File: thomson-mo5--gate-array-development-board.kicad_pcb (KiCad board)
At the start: 2 copper layers, 99.7 x 99.7 mm, 19 parts, among them J1 JTAG, J2 VPP connector, J3 5V->12V, J4 Adjustable MT3608 module, U1 4040, U2 4040, U3 GATE_ARRAY_MO5_V1_SOCKET, U4 GATE_ARRAY_MO5_V2_SOCKET, X1 XO 16MHz - DIP 8 or 14

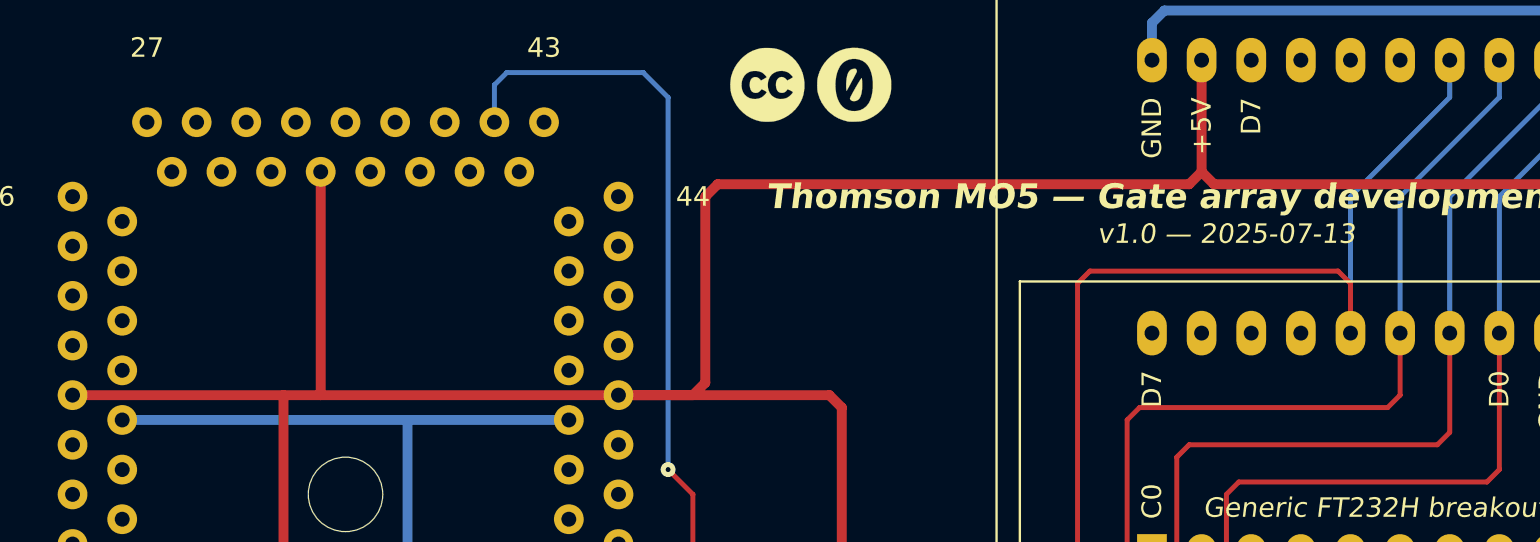
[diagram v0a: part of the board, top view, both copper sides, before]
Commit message: Fixed missing tie to ground for U3 pin 35
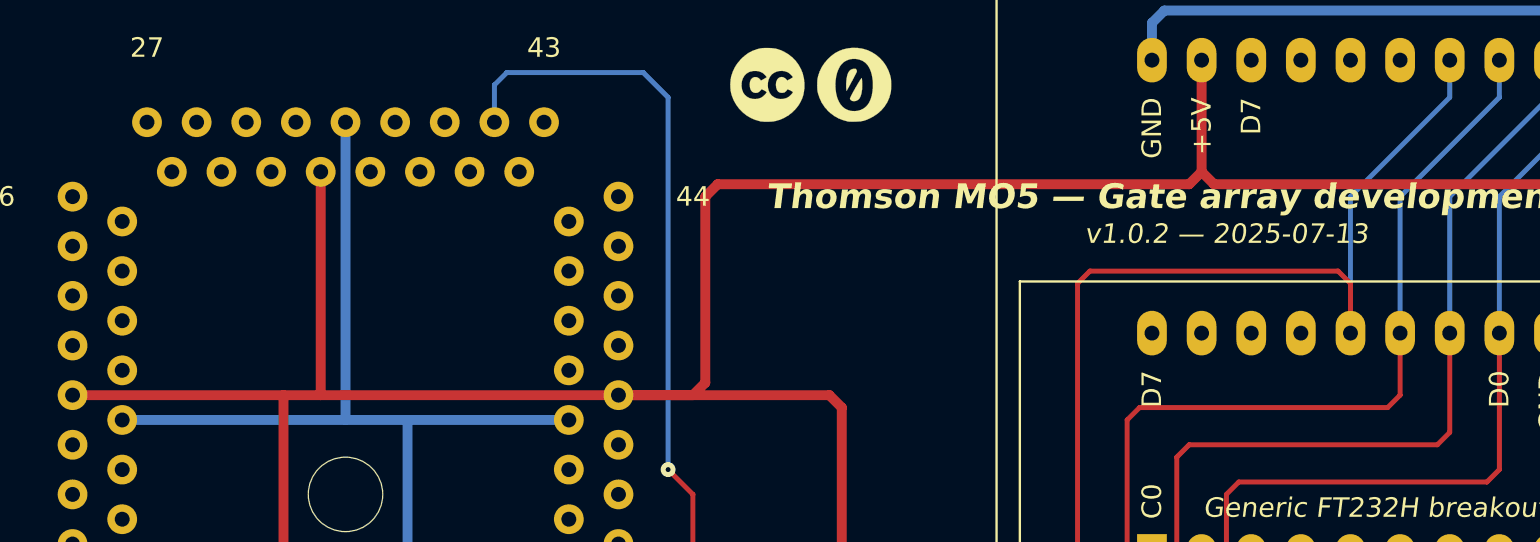
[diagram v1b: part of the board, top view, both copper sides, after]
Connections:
- U3 pad 35: unconnected-(U3-GND-Pad35) -> GND
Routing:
- net GND: track 333.4 -> 348.6 mm

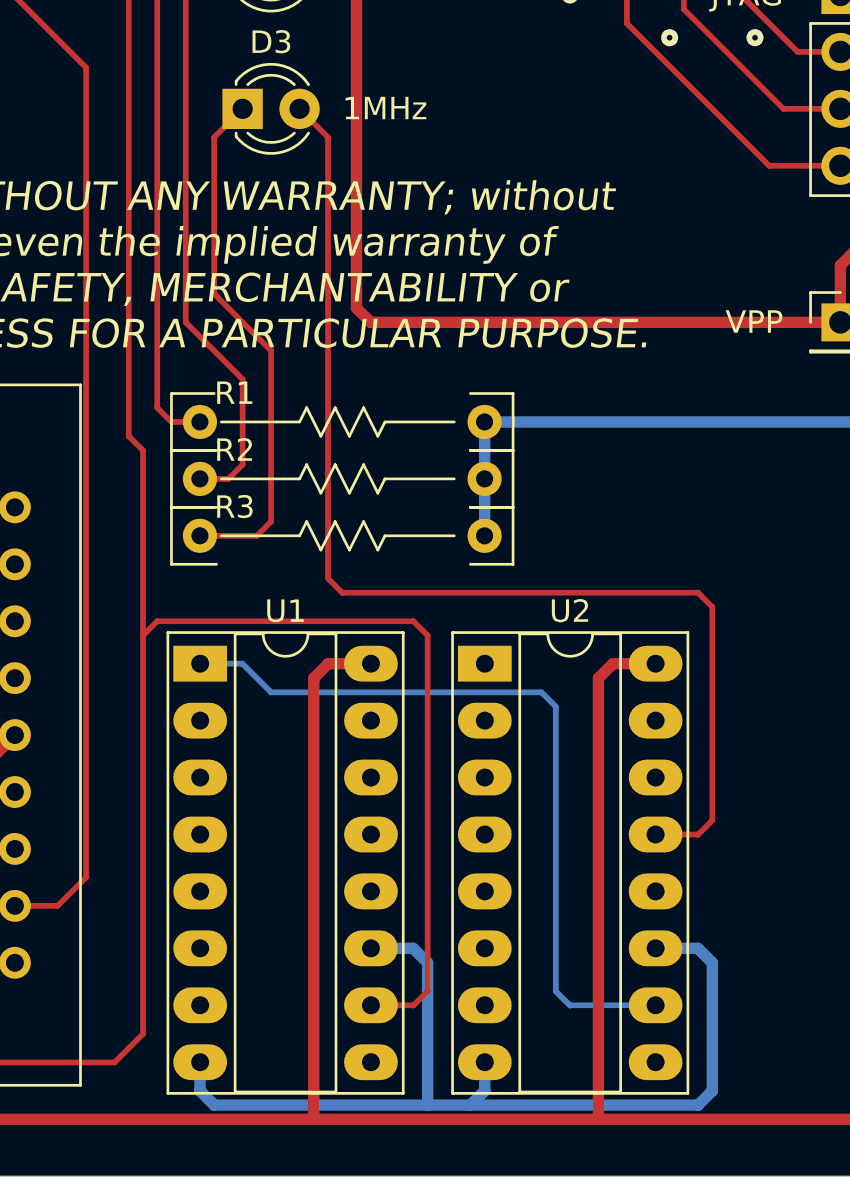
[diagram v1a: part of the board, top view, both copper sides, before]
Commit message: Fixed #1 : Missing decoupling capacitors
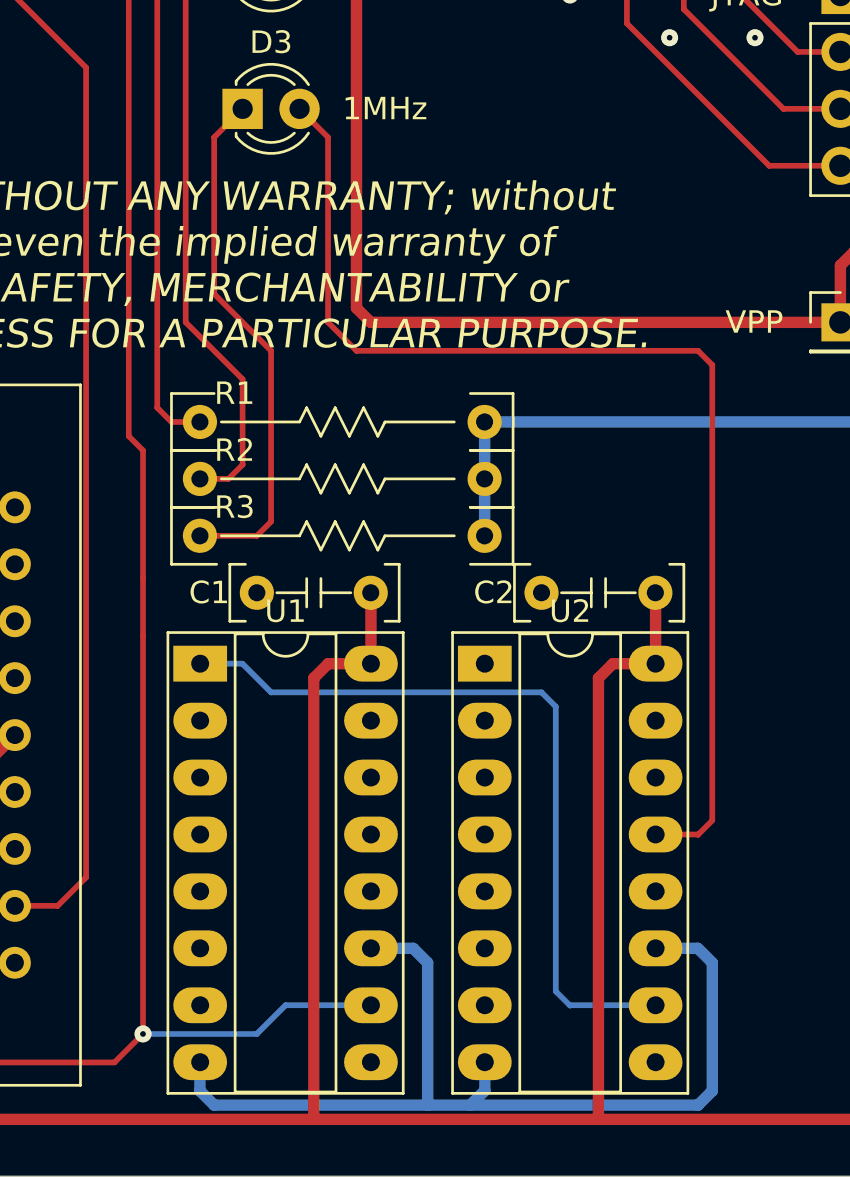
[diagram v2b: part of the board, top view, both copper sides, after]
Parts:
- added C1: 0.22uF, commons-passives_THT:Passive_THT_capacitor_mlcc_W2.54mm_L5.08mm, F.Cu at (97.2, 148.6)
- added C2: 0.22uF, commons-passives_THT:Passive_THT_capacitor_mlcc_W2.54mm_L5.08mm, F.Cu at (109.9, 148.6)
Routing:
- net E: track 144.1 -> 122.9 mm, vias 1 -> 2
- net +5V: track 433.7 -> 440.1 mm

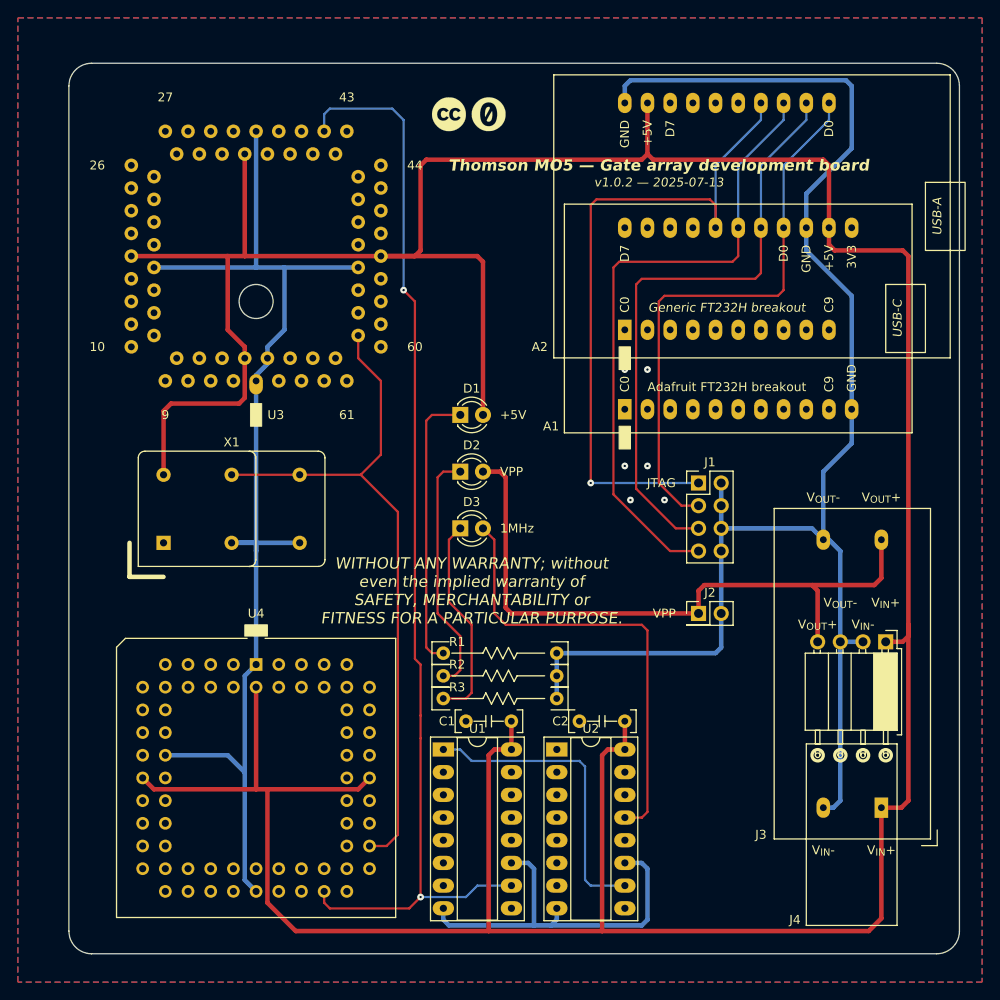
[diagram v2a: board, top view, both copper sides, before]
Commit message: orthogonal routing
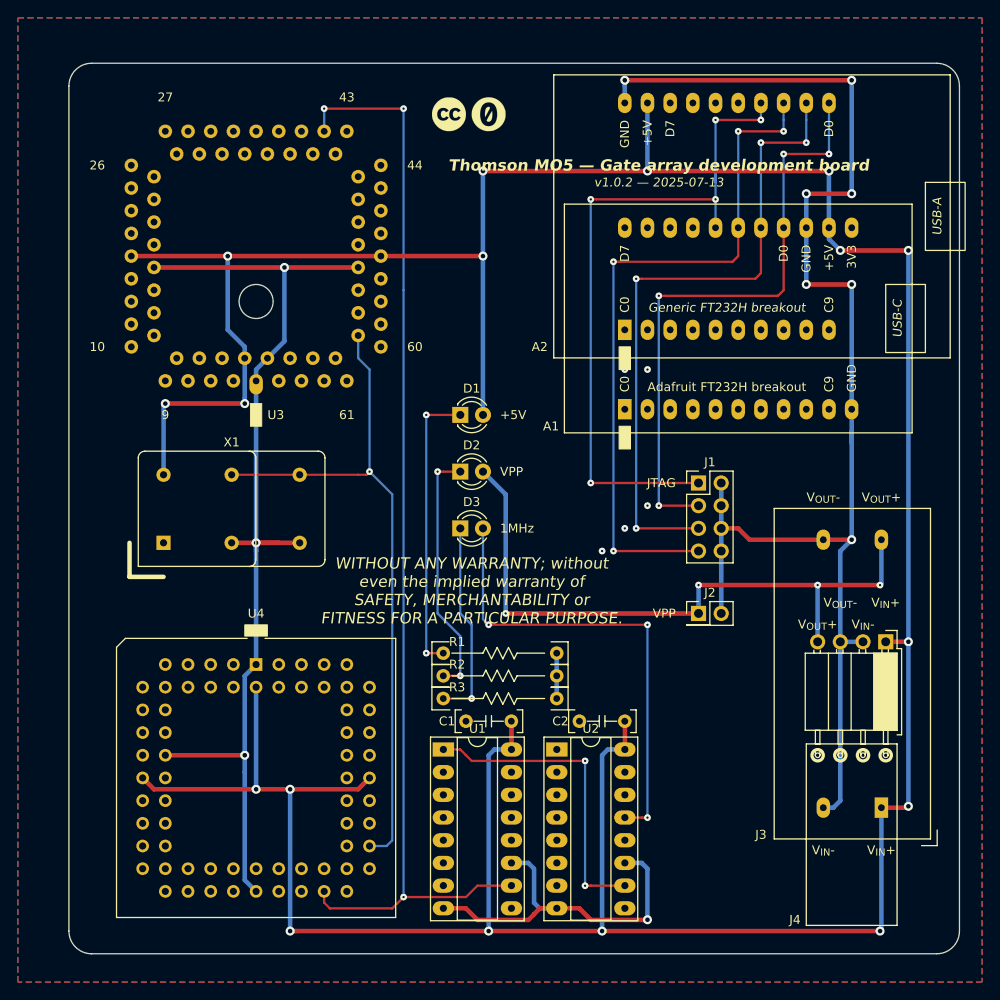
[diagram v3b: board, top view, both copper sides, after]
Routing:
- net GND: track 348.6 -> 318.0 mm, vias 6 -> 16
- net +5V: track 440.1 -> 417.2 mm, vias 0 -> 17
- net /FTDI breakouts, source JTAG, DC-DC converter/TDO: track 71.3 -> 78.4 mm, vias 0 -> 4
- net /FTDI breakouts, source JTAG, DC-DC converter/TDI: track 67.3 -> 73.3 mm, vias 0 -> 4
- net /FTDI breakouts, source JTAG, DC-DC converter/TCK: track 63.4 -> 68.2 mm, vias 0 -> 4
- net /FTDI breakouts, source JTAG, DC-DC converter/TMS: track 76.3 -> 78.7 mm, vias 1 -> 5
- net Net-(D3-A): track 51.1 -> 53.0 mm, vias 0 -> 3
- net 16MHz: track 77.7 -> 76.5 mm, vias 0 -> 1
- net Net-(D1-K): track 31.6 -> 32.4 mm, vias 0 -> 2
- net Net-(D2-K): track 27.6 -> 28.4 mm, vias 0 -> 2
- net Net-(U1-Q11): track 34.1 -> 34.8 mm, vias 0 -> 2
- net Net-(D3-K): track 23.4 -> 22.8 mm, vias 0 -> 1
- net E: track 122.9 -> 123.2 mm, vias 2 -> 3
- net +12V: track 73.8 -> 73.5 mm, vias 0 -> 4
